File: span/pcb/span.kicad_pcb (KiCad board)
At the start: 2 copper layers, 232 x 95.6 mm, 96 parts, among them J1 MJ-4PP-9, J2 MJ-4PP-9, J3 OLED, J4 OLED, SW1 SW_PUSH, SW10 SW_PUSH, SW11 SW_PUSH, SW12 SW_PUSH, SW13 SW_PUSH, SW14 SW_PUSH, SW15 SW_PUSH, SW16 SW_PUSH, SW17 SW_PUSH, SW18 SW_PUSH, SW19 SW_PUSH, SW2 SW_PUSH, SW20 SW_PUSH, SW21 SW_PUSH, SW22 SW_PUSH, SW23 SW_PUSH, SW24 SW_PUSH, SW25 SW_PUSH, SW26 SW_PUSH, SW27 SW_PUSH, SW28 SW_PUSH, SW29 SW_PUSH, SW3 SW_PUSH, SW30 SW_PUSH, SW31 SW_PUSH, SW32 SW_PUSH, SW33 SW_PUSH, SW34 SW_PUSH, SW35 SW_PUSH, SW36 SW_PUSH, SW4 SW_PUSH, SW5 SW_PUSH, SW6 SW_PUSH, SW7 SW_PUSH, SW8 SW_PUSH, SW9 SW_PUSH, U1 ProMicro, U2 ProMicro

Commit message: span: bump version
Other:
- board text added: "36dfa26"
- board text removed: "4fbf6f8"

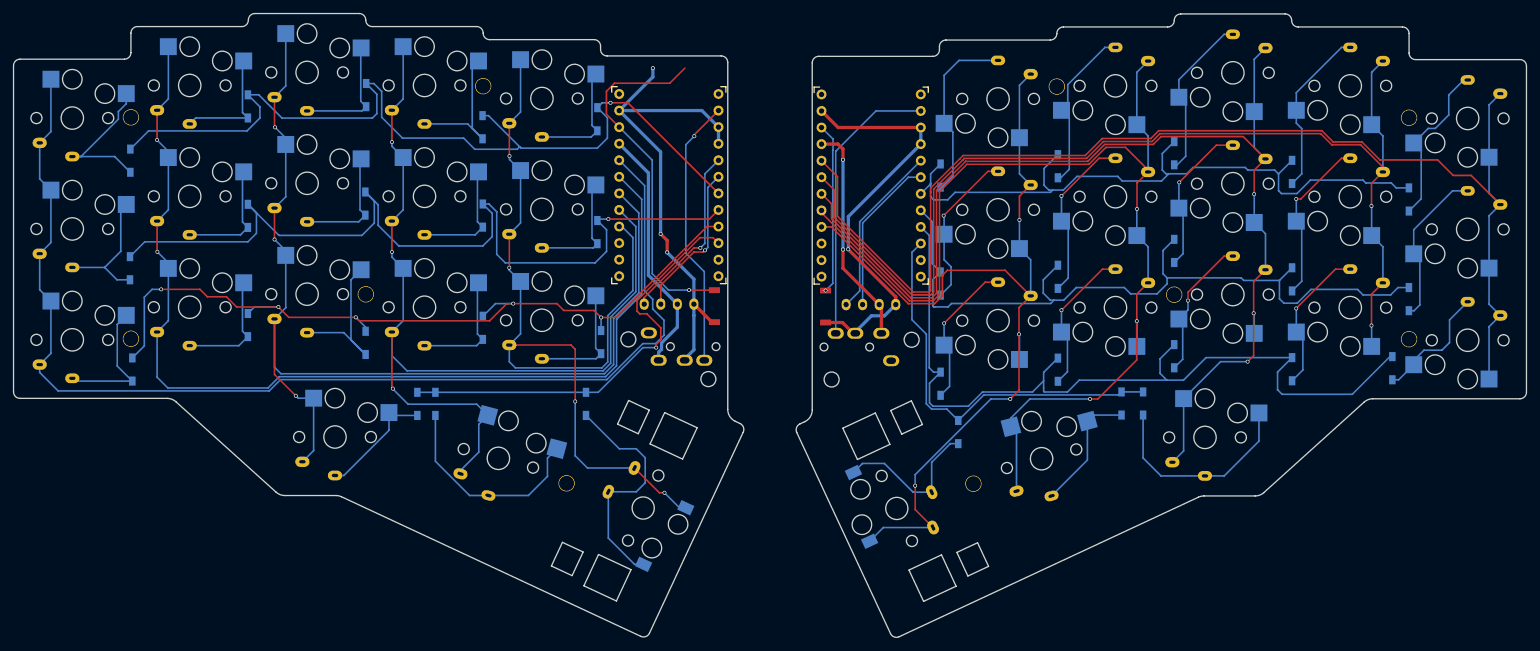
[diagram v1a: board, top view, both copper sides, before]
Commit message: span: move 2 of the thumb keys a bit
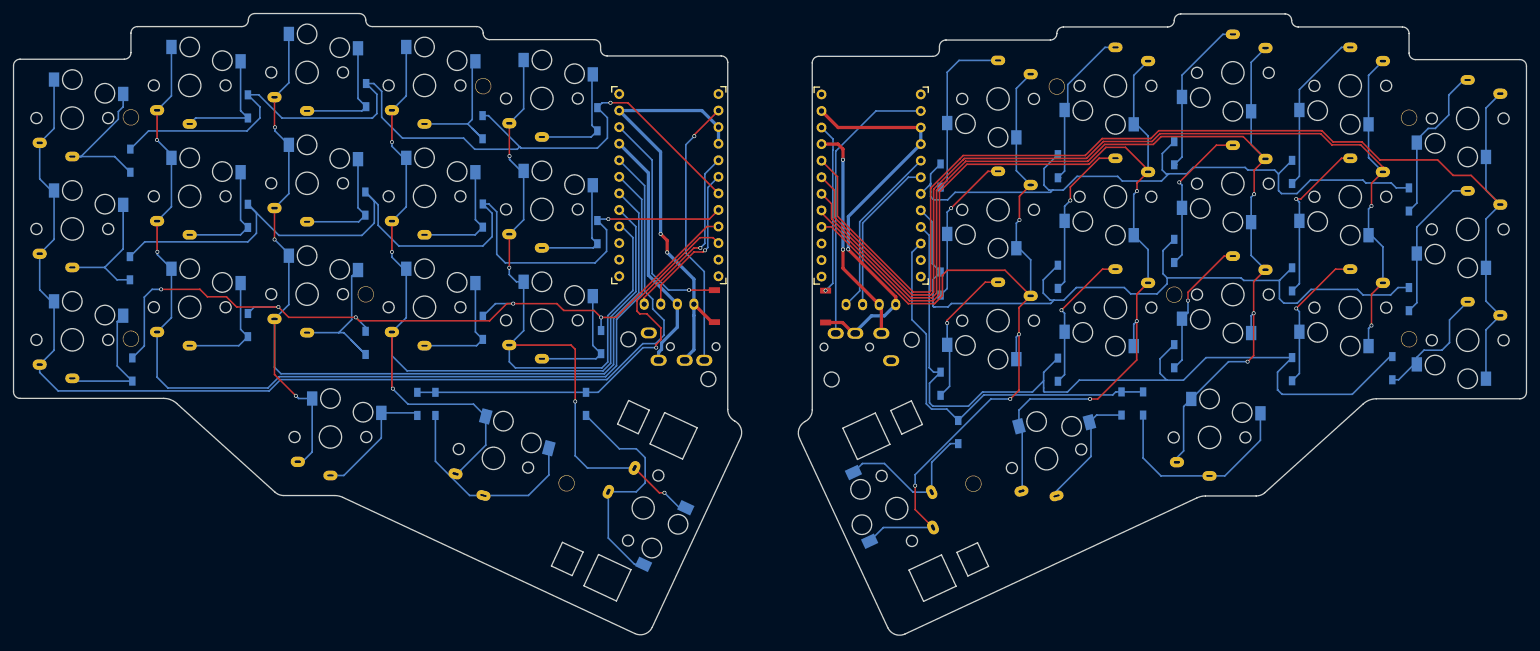
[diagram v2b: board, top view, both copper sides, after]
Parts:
- SW1, SW10, SW11, SW12, SW13, SW14, SW15, SW16, SW17, SW19, SW2, SW20, SW21, SW22, SW23, SW24, SW25, SW26, SW27, SW28, SW29, SW3, SW30, SW31, SW32, SW33, SW34, SW35, SW4, SW5, SW6, SW7, SW8, SW9: footprint keyswitches:Kailh_socket_PG1350_optional_oval_1 -> keyswitches:Kailh_socket_PG1350_optional_oval_smaller_hotswap
- moved SW35 0.76 mm to (174.0, 105.6)
- moved SW17 0.76 mm to (89.2, 105.5)
- moved SW16 0.70 mm to (64.2, 102.3)
- moved SW34 0.70 mm to (199.0, 102.3)
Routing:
- net reset: track 54.9 -> 35.2 mm
- net GND: track 140.0 -> 131.4 mm, vias 4 -> 3
- net col4: track 136.2 -> 138.0 mm
- net col0: track 178.6 -> 180.0 mm
- net Net-(D24-A): track 24.7 -> 23.4 mm
- net col1_r: track 165.7 -> 166.9 mm
- net col4_r: track 139.6 -> 140.7 mm
- net Net-(D23-A): track 27.8 -> 26.8 mm
- net Net-(D19-A): track 25.8 -> 24.8 mm
- net col1: track 158.8 -> 159.7 mm
- net col0_r: track 187.5 -> 188.4 mm
- net col3: track 147.8 -> 148.7 mm
- net Net-(D27-A): track 25.9 -> 25.1 mm
- net Net-(D22-A): track 25.8 -> 25.0 mm
- net Net-(D28-A): track 24.5 -> 23.7 mm
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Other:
- board size 232 x 95.6 mm -> 232 x 95.3 mm

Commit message: span: bump version
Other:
- board text added: "4c9eac0"
- board text removed: "36dfa26"

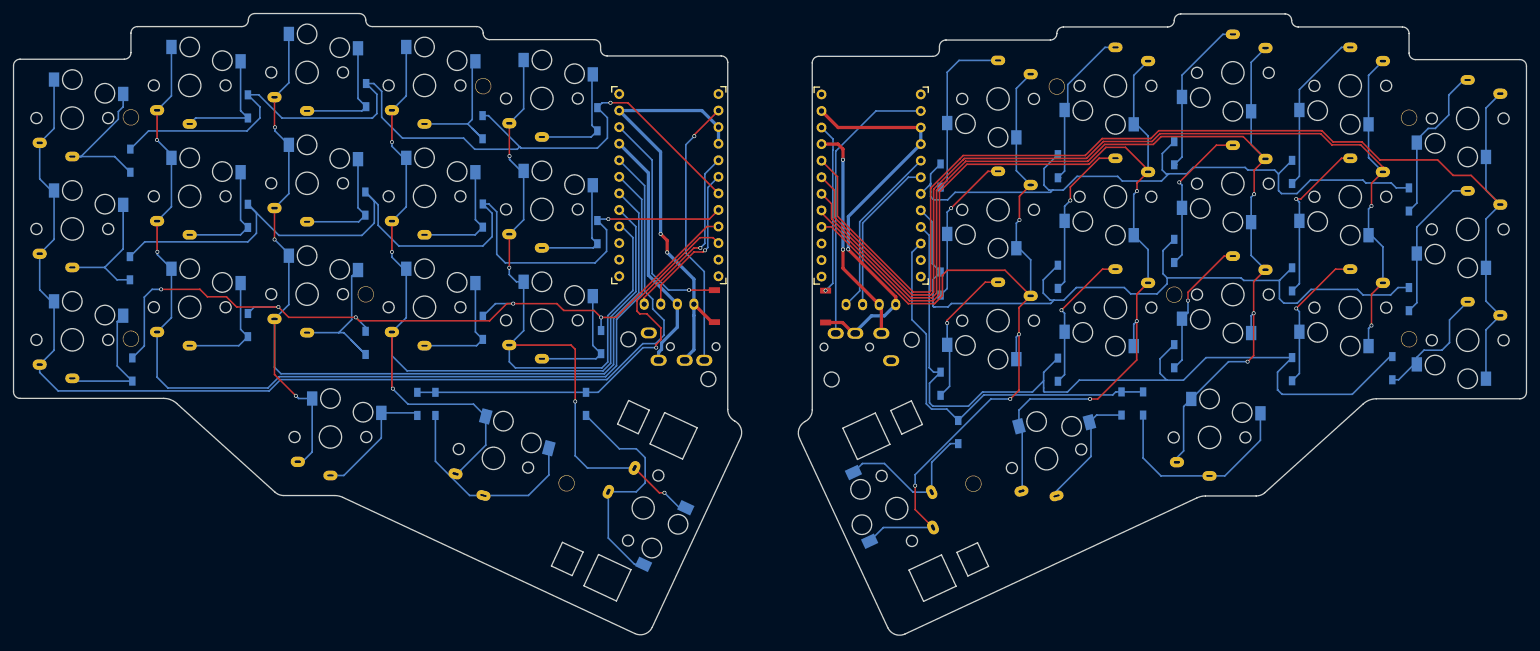
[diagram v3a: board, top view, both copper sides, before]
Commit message: span: change pcb holes to m2 spacers
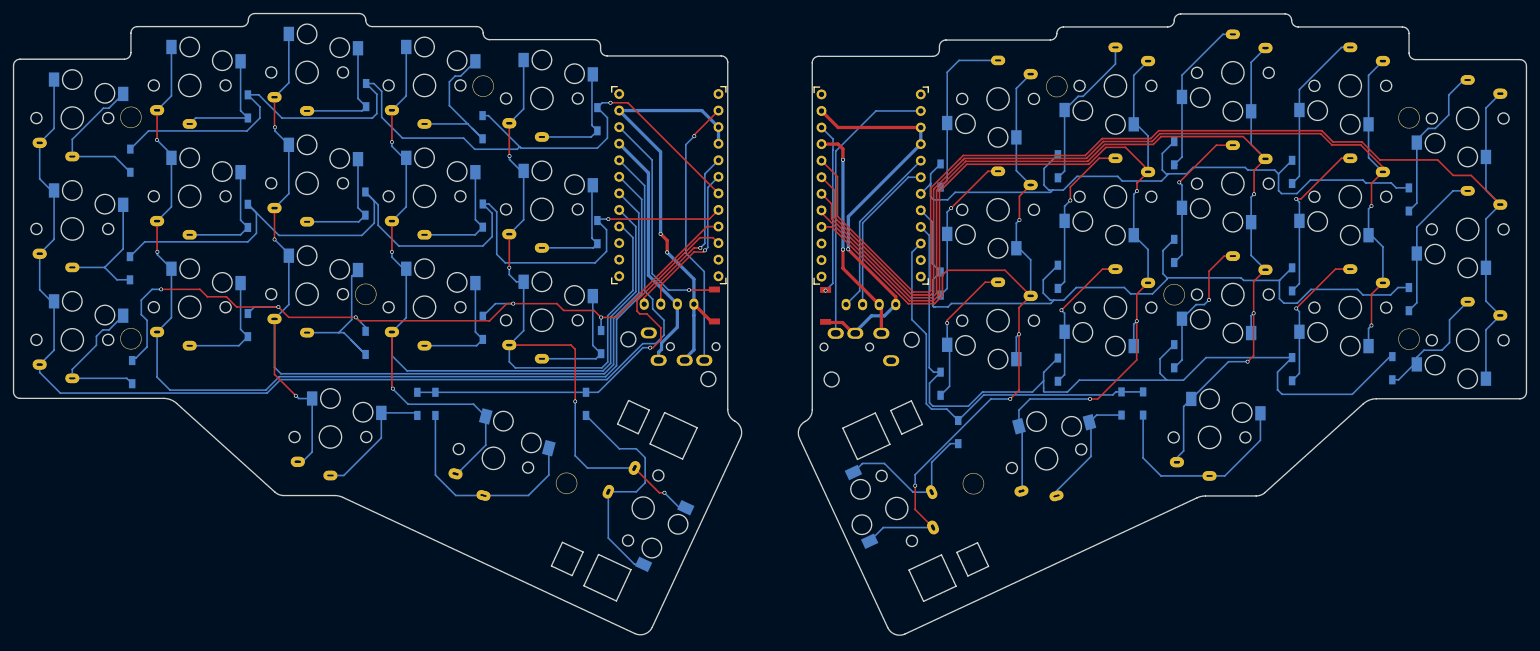
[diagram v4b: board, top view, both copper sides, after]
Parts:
- REF** (x10): value M2_HOLE -> M2_SPACER; footprint holykeebs:M2_HOLE -> holykeebs:M2_SPACER
- moved D11 0.40 mm to (33.8, 92.3)
- moved RSW1 0.10 mm to (123.1, 82.1)
- moved RSW2 0.10 mm to (140.1, 82.2)
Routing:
- net Net-(D4-A): track 22.2 -> 25.0 mm
- net Net-(D11-A): track 20.7 -> 23.5 mm
- net Net-(D17-A): track 32.0 -> 33.2 mm
- net row2: track 123.7 -> 124.7 mm
- net Net-(D31-A): track 21.6 -> 22.4 mm
- net Net-(D22-A): track 25.0 -> 24.5 mm

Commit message: span: bump version
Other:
- board text added: "2da5623"
- board text removed: "4c9eac0"

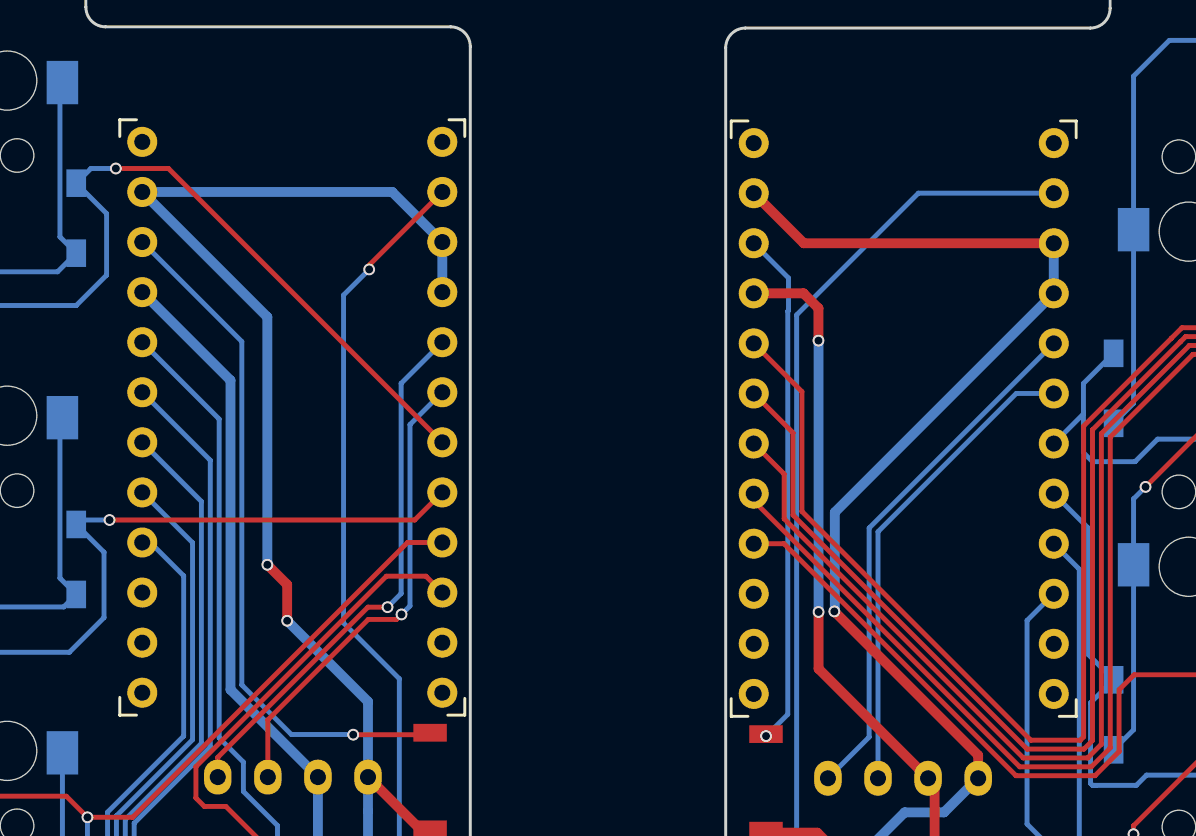
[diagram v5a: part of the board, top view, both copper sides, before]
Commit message: add span changes before deleting due to move to separate repo
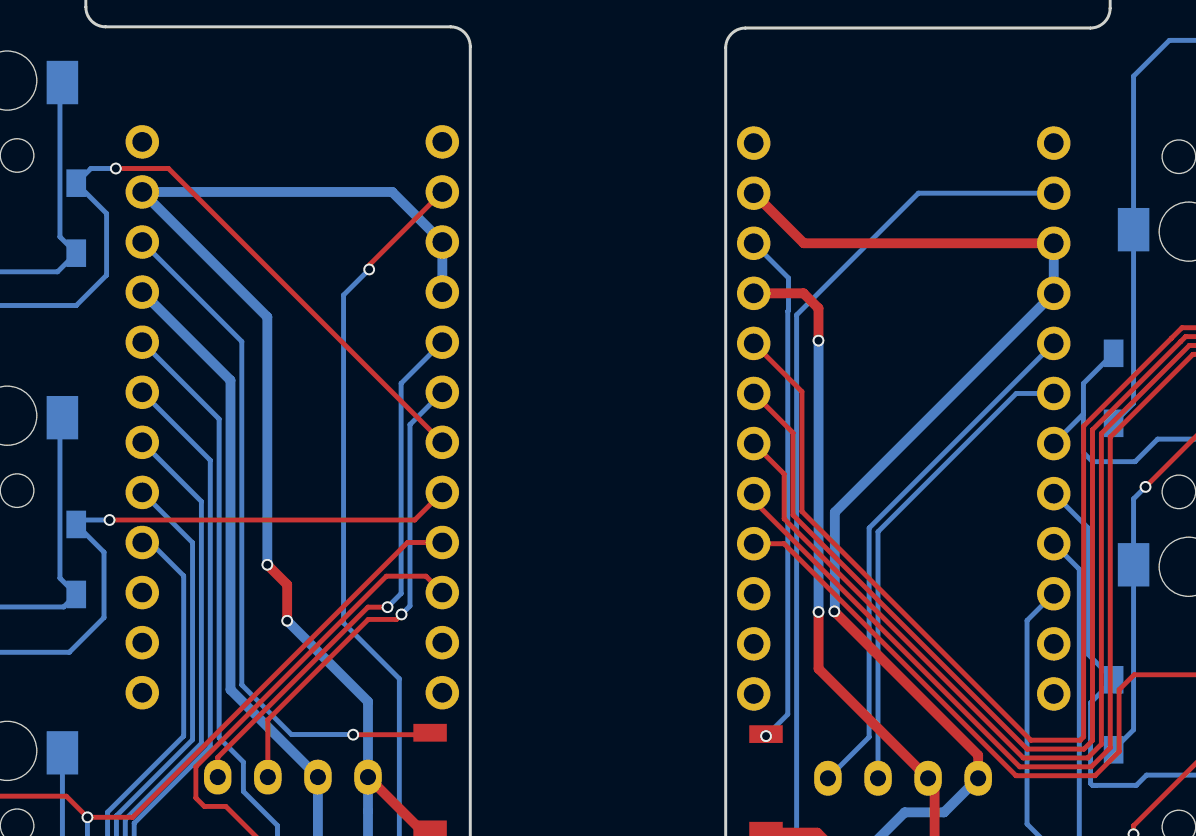
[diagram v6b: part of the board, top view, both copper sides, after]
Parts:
- U1, U2: footprint kbd:ProMicro_v3 -> holykeebs:ProMicro_1mm_holes
